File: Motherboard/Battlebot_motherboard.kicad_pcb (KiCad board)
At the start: 2 copper layers, 12 x 20.6 mm, 5 parts, among them Q1 IRLZ44N, Q2 IRLZ44N, U1 rp2040-zero

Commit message: all the pcb stuff
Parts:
- removed CR1, CR2: L6203, footprints:Multiwatt11_V_STM
- removed Q1, Q2: IRLZ44N, Package_TO_SOT_THT:TO-220-3_Vertical
- removed U1: rp2040-zero, footprints:rp2040-zero-tht
- added ?: , , F.Cu at (158.8, 64.5)
- added ?: , , F.Cu at (165.2, 91.8)
- added ?: , , F.Cu at (165.5, 65.0)
- added ?: , , F.Cu at (167.5, 96.2)
- added ?: , , F.Cu at (158.8, 81.2)
- added ?: , , F.Cu at (175.0, 77.8)
- added ?: , , F.Cu at (164.8, 67.0)
- added ?: , , F.Cu at (165.0, 89.2)
- added ?: , , F.Cu at (156.2, 99.0)
- added ?: , , F.Cu at (171.2, 93.5)
- added ?: , , F.Cu at (186.2, 80.8)
- added ?: , , F.Cu at (162.8, 68.5)
- added C1: 100nF, Capacitor_SMD:C_0805_2012Metric_Pad1.18x1.45mm_HandSolder, F.Cu at (150.8, 92.0)
- added C10: 1uF, Capacitor_SMD:C_0805_2012Metric_Pad1.18x1.45mm_HandSolder, F.Cu at (174.0, 82.0)
- added C11: 100uF, Capacitor_SMD:CP_Elec_3x5.3, F.Cu at (164.5, 78.0)
- added C12: 100uF, Capacitor_SMD:CP_Elec_3x5.3, F.Cu at (172.2, 78.0)
- added C2: 100nF, Capacitor_SMD:C_0805_2012Metric_Pad1.18x1.45mm_HandSolder, F.Cu at (181.5, 103.0)
- added C3: 10nF, Capacitor_SMD:C_0805_2012Metric_Pad1.18x1.45mm_HandSolder, F.Cu at (149.5, 80.5)
- added C4: 10nF, Capacitor_SMD:C_0805_2012Metric_Pad1.18x1.45mm_HandSolder, F.Cu at (177.0, 102.0)
- added C5: 10nF, Capacitor_SMD:C_0805_2012Metric_Pad1.18x1.45mm_HandSolder, F.Cu at (163.8, 73.0)
- added C6: 10nF, Capacitor_SMD:C_0805_2012Metric_Pad1.18x1.45mm_HandSolder, F.Cu at (178.0, 81.5)
- added C7: 100nF, Capacitor_SMD:C_0805_2012Metric_Pad1.18x1.45mm_HandSolder, F.Cu at (152.2, 83.5)
- added C8: 100nF, Capacitor_SMD:C_0805_2012Metric_Pad1.18x1.45mm_HandSolder, F.Cu at (174.0, 84.5)
- added C9: 1uF, Capacitor_SMD:C_0805_2012Metric_Pad1.18x1.45mm_HandSolder, F.Cu at (154.5, 80.0)
- added J1: R_1206_3216Metric, Resistor_SMD:R_1206_3216Metric, F.Cu at (169.0, 80.2)
- added J1: BEC, Connector_PinHeader_2.54mm:PinHeader_1x03_P2.54mm_Vertical, F.Cu at (187.0, 72.5)
- added J2: Reciever, Connector_PinHeader_2.54mm:PinHeader_1x03_P2.54mm_Vertical, F.Cu at (154.5, 55.0)
- added J3: 12Vin, library:2_Wire, F.Cu at (157.5, 71.0)
- added J4: Conn_01x02_Socket, library:2_Wire, F.Cu at (157.5, 76.5)
- added J5: Conn_01x02_Socket, library:2_Wire, F.Cu at (157.5, 65.5)
- added J6: Fan connector, Connector_JST:JST_PH_S2B-PH-K_1x02_P2.00mm_Horizontal, F.Cu at (183.1, 68.0)
- added JP1: 0ohm, Resistor_SMD:R_1206_3216Metric_Pad1.30x1.75mm_HandSolder, F.Cu at (108.0, 65.2)
- added JP2: 0ohm, Resistor_SMD:R_1206_3216Metric_Pad1.30x1.75mm_HandSolder, F.Cu at (108.0, 68.5)
- added R1: 10kohm, Resistor_SMD:R_0805_2012Metric_Pad1.20x1.40mm_HandSolder, F.Cu at (165.0, 96.2)
- added R2: 10kohm, Resistor_SMD:R_0805_2012Metric_Pad1.20x1.40mm_HandSolder, F.Cu at (173.5, 89.5)
- added R3: 22kohm, Resistor_SMD:R_0805_2012Metric_Pad1.20x1.40mm_HandSolder, F.Cu at (163.0, 82.0)
- added R4: 22kohm, Resistor_SMD:R_0805_2012Metric_Pad1.20x1.40mm_HandSolder, F.Cu at (183.5, 80.5)
- added R5: 10kohm, Resistor_SMD:R_0805_2012Metric_Pad1.20x1.40mm_HandSolder, F.Cu at (163.0, 84.0)
- added R6: 10kohm, Resistor_SMD:R_0805_2012Metric_Pad1.20x1.40mm_HandSolder, F.Cu at (181.5, 80.5)
- added REF**: BoardOutline, footprints:BoardOutline, F.Cu at (168.5, 78.0)
- added U2: L9958SBTR, footprints:POWERSO16_STM, F.Cu at (157.5, 90.0)
- added U3: L9958SBTR, footprints:POWERSO16_STM, F.Cu at (179.5, 91.5)
- added U4: XIAO-RP2040-SMD, footprints:XIAO-RP2040-SMD, F.Cu at (171.5, 54.0)
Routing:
- net +5V: track 0.00 -> 130.4 mm
- net PWM1: track 0.00 -> 69.3 mm
- net Net-(J5-Pin_2): track 0.00 -> 65.6 mm
- net DIR1: track 0.00 -> 61.3 mm
- net 1SO: track 0.00 -> 46.2 mm
- net µSO: track 0.00 -> 41.8 mm
- net +12V: track 0.00 -> 35.6 mm
- net PWM3: track 0.00 -> 34.3 mm
- net PWM2: track 0.00 -> 32.4 mm
- net SCK: track 0.00 -> 29.1 mm
- net Net-(U2-OUT1): track 0.00 -> 27.4 mm
- net CS: track 0.00 -> 26.8 mm
- net DIR2: track 0.00 -> 26.3 mm
- net PPM: track 0.00 -> 26.2 mm
- net Net-(J1-Pin_2): track 0.00 -> 17.6 mm
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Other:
- board size 12 x 20.6 mm -> 42 x 61.5 mm

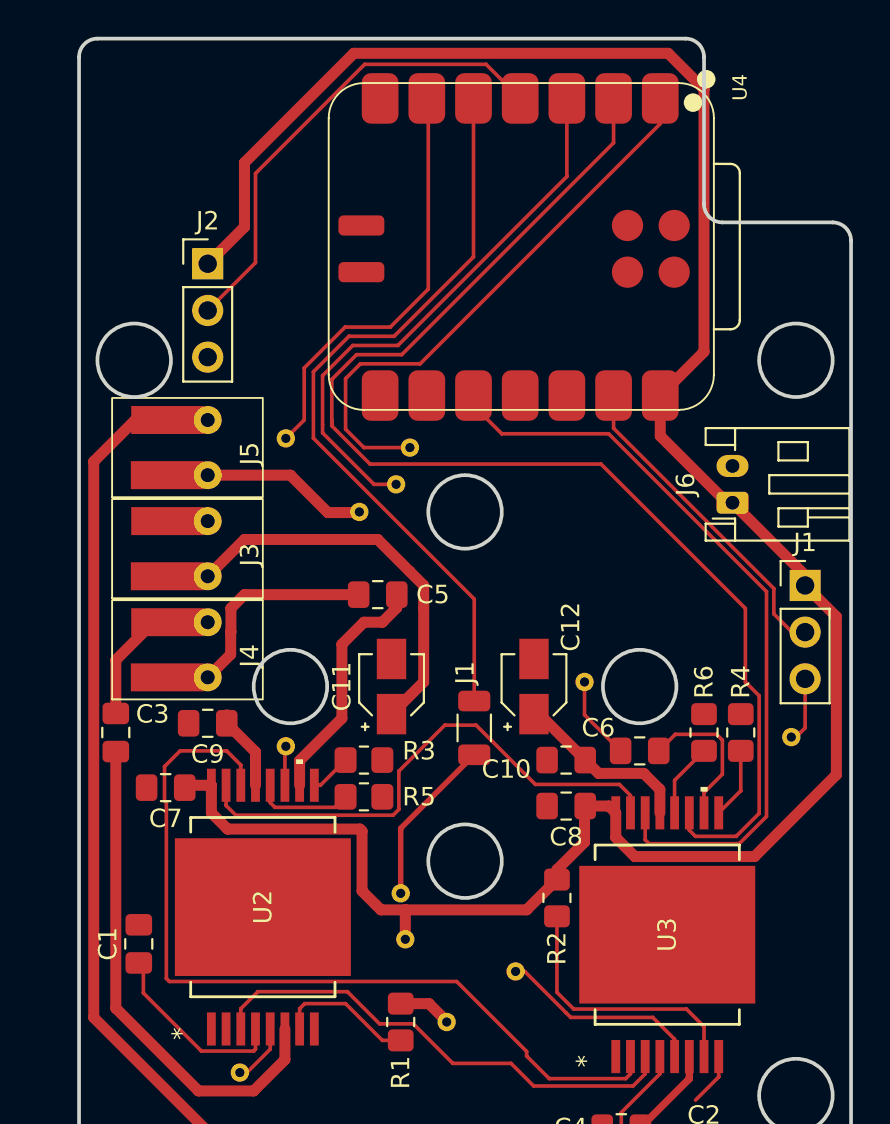
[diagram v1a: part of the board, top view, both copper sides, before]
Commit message: Update schematic which was quite wrong in a number of places
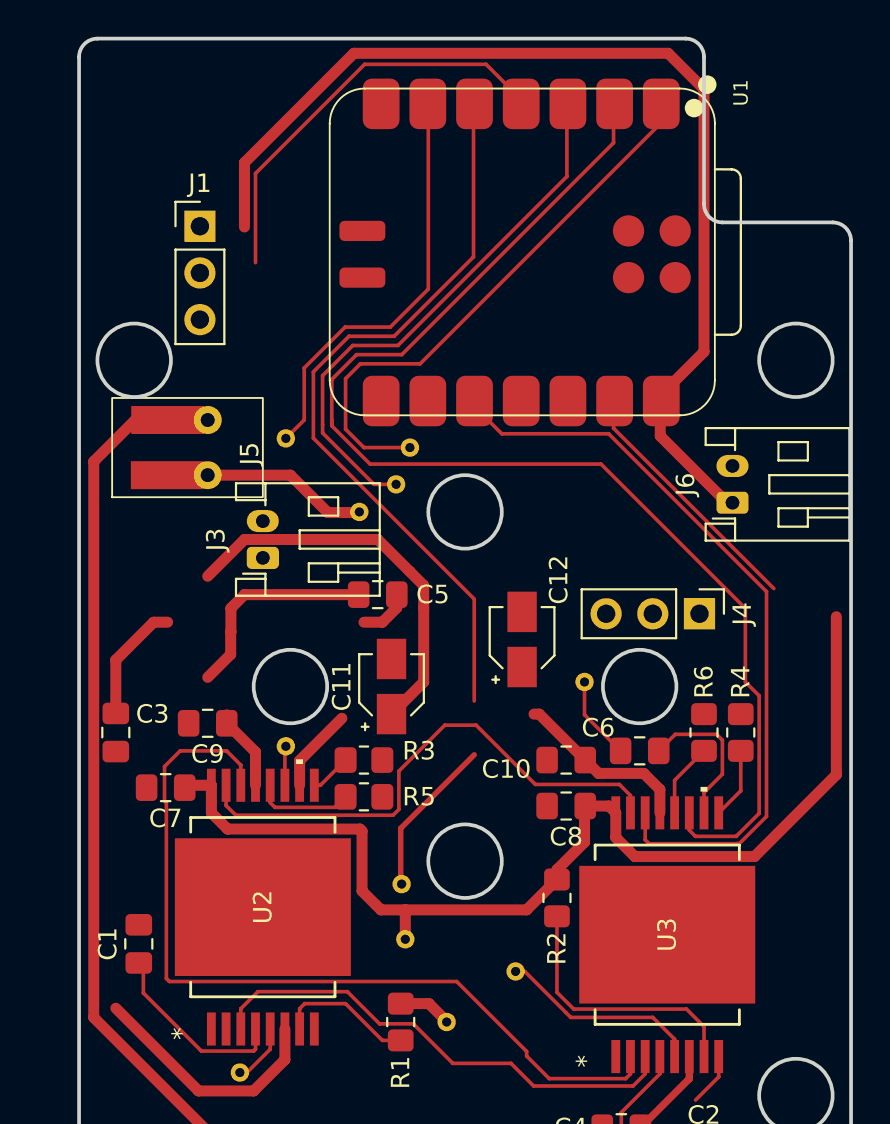
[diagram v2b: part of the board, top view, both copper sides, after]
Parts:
- removed the ? at (186.2, 80.8)
- removed the J1 at (169.0, 80.2)
- removed the J1 at (187.0, 72.5)
- removed J2: Reciever, Connector_PinHeader_2.54mm:PinHeader_1x03_P2.54mm_Vertical
- removed U4: XIAO-RP2040-SMD, footprints:XIAO-RP2040-SMD
- added J1: Reciever, Connector_PinHeader_2.54mm:PinHeader_1x03_P2.54mm_Vertical, F.Cu at (154.1, 53.0)
- added U1: XIAO-RP2040-SMD, footprints:XIAO-RP2040-SMD, F.Cu at (171.6, 54.3)
- J3: value 12Vin -> Fan connector; footprint library:2_Wire -> Connector_JST:JST_PH_S2B-PH-K_1x02_P2.00mm_Horizontal
- J4: value Conn_01x02_Socket -> BEC; footprint library:2_Wire -> Connector_PinHeader_2.54mm:PinHeader_1x03_P2.54mm_Vertical
- moved J4 23.9 mm to (181.3, 74.0), turned to -90 degrees
- moved C12 2.64 mm to (171.6, 75.4)
- moved ? 0.50 mm to (165.0, 88.7)
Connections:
- net DI1 renamed Net-(U3-DI)
- C1 pad 2: GND -> +12V
- C2 pad 2: GND -> +12V
- C3 pad 1: Net-(U2-OUT1) -> Net-(J5-Pin_2)
- C3 pad 2: Net-(J4-Pin_2) -> GND
- C4 pad 1: Net-(U3-OUT1) -> Net-(J6-Pin_2)
- C4 pad 2: Net-(J5-Pin_2) -> GND
- C5 pad 1: Net-(J4-Pin_1) -> GND
- C5 pad 2: Net-(U2-OUT2) -> Net-(J5-Pin_1)
- C6 pad 1: Net-(J5-Pin_1) -> GND
- C6 pad 2: Net-(U3-OUT2) -> Net-(J6-Pin_1)
- J3 pad 1: +12V -> +5V
- J4 pad 1: Net-(J4-Pin_1) -> +5V
- R1 pad 1: DI2 -> unconnected-(R1-Pad1)
- U2 pad 10: Net-(U2-OUT2) -> Net-(J6-Pin_1)
- U2 pad 6: Net-(U2-OUT1) -> Net-(J6-Pin_2)
- U2 pad 7: DI2 -> unconnected-(U2-DI-Pad7)
- U3 pad 10: Net-(U3-OUT2) -> Net-(J5-Pin_1)
- U3 pad 6: Net-(U3-OUT1) -> Net-(J5-Pin_2)
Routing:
- net Net-(U2-OUT1): track 27.4 -> 0.00 mm
- net GND: track 2.89 -> 25.6 mm
- net (no net): track 0.00 -> 20.9 mm
- net Net-(J1-Pin_2): track 17.6 -> 0.00 mm
- net Net-(J6-Pin_2): track 0.00 -> 13.4 mm
- net Net-(U2-OUT2): track 13.1 -> 0.00 mm
- net Net-(J4-Pin_1): track 11.5 -> 0.00 mm
- net +5V: track 130.4 -> 119.0 mm
- net Net-(U3-OUT2): track 8.34 -> 0.00 mm
- net DI2: track 7.54 -> 0.00 mm
- net Net-(J4-Pin_2): track 6.58 -> 14.1 mm
- net Net-(U3-OUT1): track 4.97 -> 0.00 mm
- net Net-(J6-Pin_1): track 0.00 -> 4.60 mm
- net PPM: track 26.2 -> 22.5 mm
- net PWM3: track 34.3 -> 30.9 mm
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
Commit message: nightmare routing job
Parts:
- removed the ? at (158.8, 64.5)
- removed the ? at (165.5, 65.0)
- removed the ? at (167.5, 96.2)
- removed the ? at (158.8, 81.2)
- removed the ? at (175.0, 77.8)
- removed the ? at (164.8, 67.0)
- removed the ? at (165.0, 88.7)
- removed the ? at (156.2, 99.0)
- removed the ? at (171.2, 93.5)
- removed the ? at (162.8, 68.5)
- removed the ? at (165.2, 91.8)
- removed the J3 at (157.5, 71.0)
- removed JP1, JP2: 0ohm, Resistor_SMD:R_1206_3216Metric_Pad1.30x1.75mm_HandSolder
- added ?: , , F.Cu at (157.8, 65.2)
- added ?: , , F.Cu at (162.8, 100.8)
- added ?: , , F.Cu at (172.8, 83.0)
- added ?: , , F.Cu at (185.2, 47.8)
- added ?: , , F.Cu at (171.5, 81.5)
- added ?: , , F.Cu at (184.0, 81.8)
- added ?: , , F.Cu at (183.5, 99.8)
- added ?: , , F.Cu at (166.8, 101.8)
- added ?: , , F.Cu at (161.8, 79.0)
- added ?: , , F.Cu at (157.8, 71.8)
- added ?: , , F.Cu at (178.5, 100.8)
- added ?: , , F.Cu at (185.2, 49.5)
- added ?: , , F.Cu at (163.0, 65.8)
- added ?: , , F.Cu at (157.8, 70.0)
- added ?: , , F.Cu at (185.2, 51.2)
- added ?: , , F.Cu at (156.0, 81.2)
- added ?: , , F.Cu at (185.2, 46.0)
- added ?: , , F.Cu at (157.8, 67.0)
- added ?: , , F.Cu at (165.2, 65.8)
- added ?: , , F.Cu at (173.0, 66.0)
- added ?: , , F.Cu at (154.5, 99.8)
- added ?: , , F.Cu at (165.2, 67.5)
- added ?: , , F.Cu at (175.0, 66.0)
- added ?: , , F.Cu at (162.2, 97.0)
- added J2: 12Vin, library:2_Wire, F.Cu at (157.0, 60.8)
- added J6: Conn_01x02_Socket, Connector_JST:JST_PH_S2B-PH-K_1x02_P2.00mm_Horizontal, F.Cu at (154.5, 73.0)
- added REF**: PinHeader_1x01_P2.54mm_Vertical, Connector_PinHeader_2.54mm:PinHeader_1x01_P2.54mm_Vertical, F.Cu at (185.2, 53.0)
- J5: footprint library:2_Wire -> Connector_JST:JST_PH_S2B-PH-K_1x02_P2.00mm_Horizontal
- REF**: moved to B.Cu
- moved J4 31.3 mm to (156.2, 55.2)
- moved C3 30.6 mm to (171.2, 102.0), turned to 180 degrees
- moved C5 19.5 mm to (181.8, 80.5), turned to -90 degrees
- moved C6 18.0 mm to (160.0, 81.0), turned to 180 degrees
- moved C4 15.8 mm to (161.5, 99.0), turned to 0 degrees
- moved R2 15.4 mm to (182.8, 101.8), turned to 0 degrees
- moved C10 11.3 mm to (185.0, 84.8), turned to 0 degrees
- moved J1 9.84 mm to (158.5, 44.2)
- moved C2 9.09 mm to (173.8, 98.2), turned to 180 degrees
- moved R1 8.10 mm to (163.8, 88.2)
- moved R6 3.26 mm to (178.2, 80.2), turned to 180 degrees
- moved J5 3.04 mm to (154.5, 66.0), turned to -90 degrees
- moved R4 3.02 mm to (186.2, 81.8)
- moved C12 2.70 mm to (173.0, 77.8)
- moved R3 1.03 mm to (164.0, 81.8)
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- renumbered J6 to J3
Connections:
- R1 pad 1: unconnected-(R1-Pad1) -> Net-(U2-DI)
- U2 pad 7: unconnected-(U2-DI-Pad7) -> Net-(U2-DI)
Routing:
- net +5V: track 119.0 -> 225.6 mm
- net +12V: track 35.6 -> 85.7 mm
- net Net-(J5-Pin_2): track 65.6 -> 22.6 mm
- net DIR1: track 61.3 -> 22.7 mm
- net µSO: track 41.8 -> 14.5 mm
- net GND: track 25.6 -> 0.00 mm
- net PWM3: track 30.9 -> 6.20 mm
- net (no net): track 20.9 -> 0.00 mm
- net PWM2: track 32.4 -> 12.6 mm
- net PWM1: track 69.3 -> 50.8 mm
- net SCK: track 29.1 -> 13.9 mm
- net 1SO: track 46.2 -> 32.5 mm
- net Net-(J4-Pin_2): track 14.1 -> 26.1 mm
- net Net-(U3-DI): track 14.5 -> 3.72 mm
- net Net-(U2-DI): track 0.00 -> 10.3 mm
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- added copper zone on F.Cu, net GND
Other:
- outline, holes or cut-outs redrawn

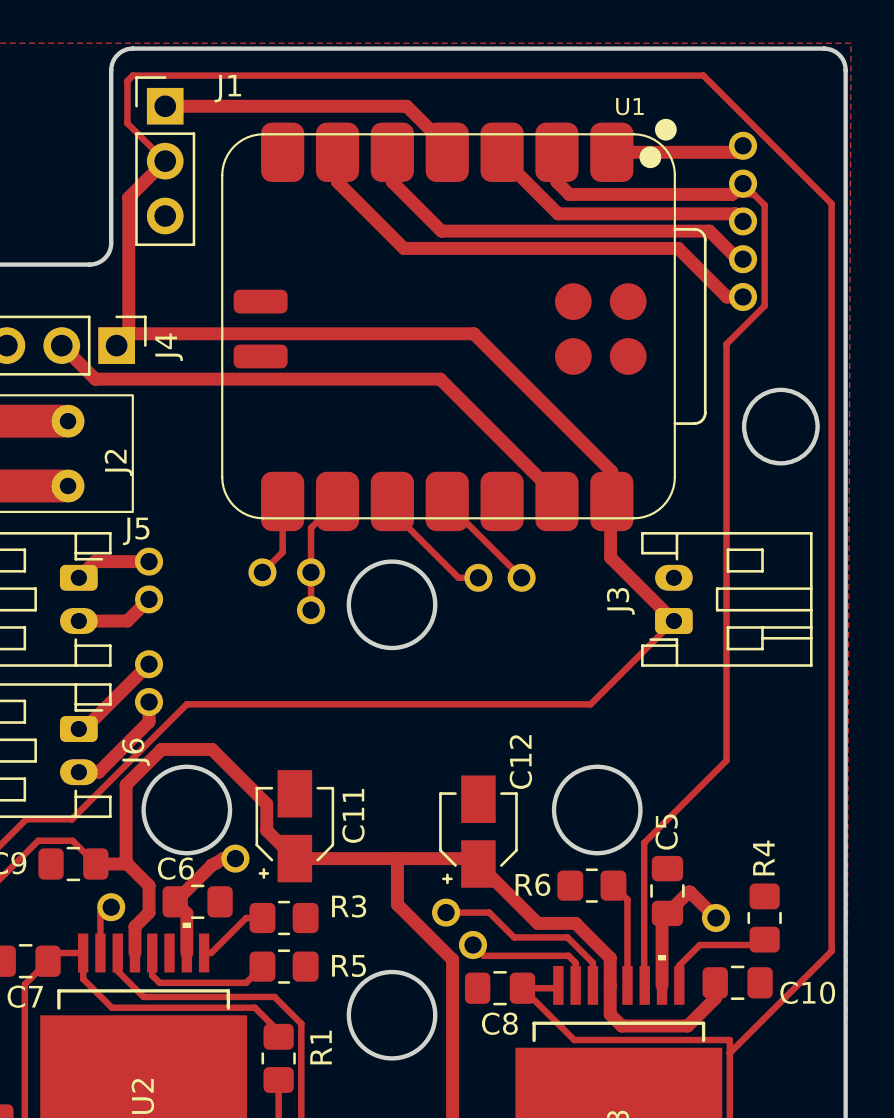
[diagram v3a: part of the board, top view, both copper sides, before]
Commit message: moved some jumper holes for usb access
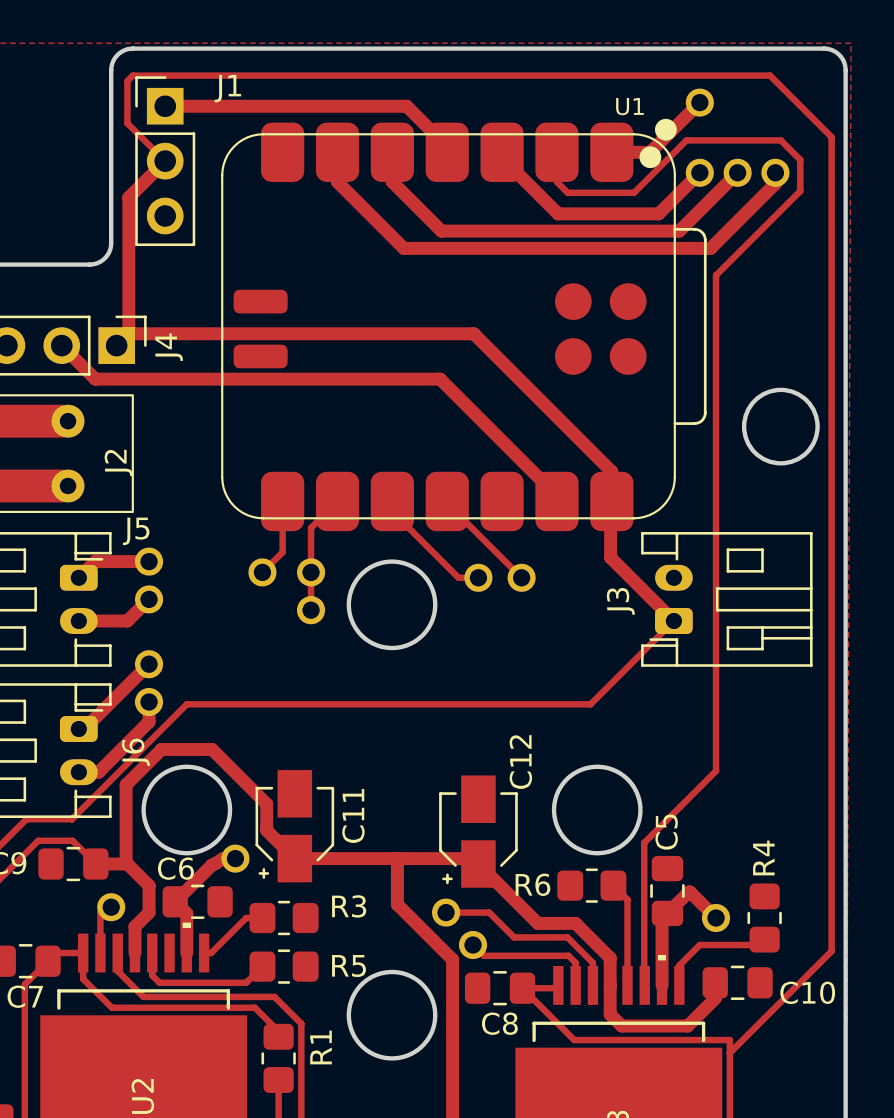
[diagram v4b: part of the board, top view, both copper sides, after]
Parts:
- removed the ? at (185.2, 47.8)
- moved REF** 5.94 mm to (186.8, 47.2)
- moved ? 4.01 mm to (185.0, 47.2)
- moved ? 3.01 mm to (183.2, 47.2)
- moved ? 2.83 mm to (183.2, 44.0)
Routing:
- net PWM1: track 50.8 -> 55.4 mm
- net DIR2: track 29.8 -> 32.1 mm
- net +5V: track 225.6 -> 227.4 mm
- net PWM2: track 12.6 -> 11.3 mm
- net PWM3: track 6.20 -> 5.03 mm
